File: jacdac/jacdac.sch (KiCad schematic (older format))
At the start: 6 parts, among them J1 Conn_02x03_Odd_Even, J2 Conn_02x03_Odd_Even

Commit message: update schematic to audio TRRS
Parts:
- removed J? (x3): AudioJackSwitch, symbol Connector:AudioJack3_Ground_Switch
- removed J?: AudioJack4_Ground, symbol Connector:AudioJack4_Ground
- added J3, J4, J5, J6: Audio_Jack_TRRS, Connectors:AUDIO-JACK-TRRS-SMD, symbol Connector:Audio_Jack_TRRS
- J1, J2: footprint (none) -> Pines:62000621121
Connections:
- wire segments 36 -> 39
- no-connect marks 7 -> 4

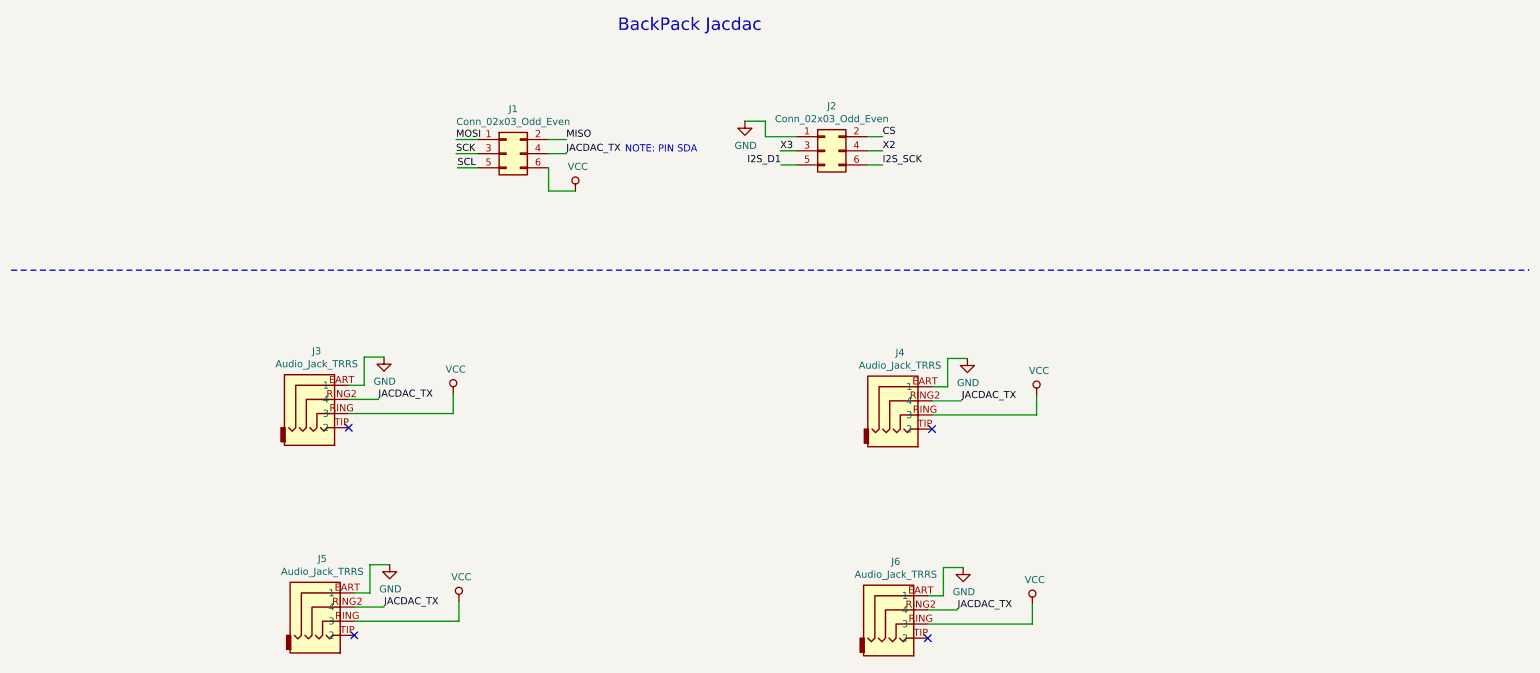
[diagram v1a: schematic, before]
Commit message: fix pin number jack TRRS
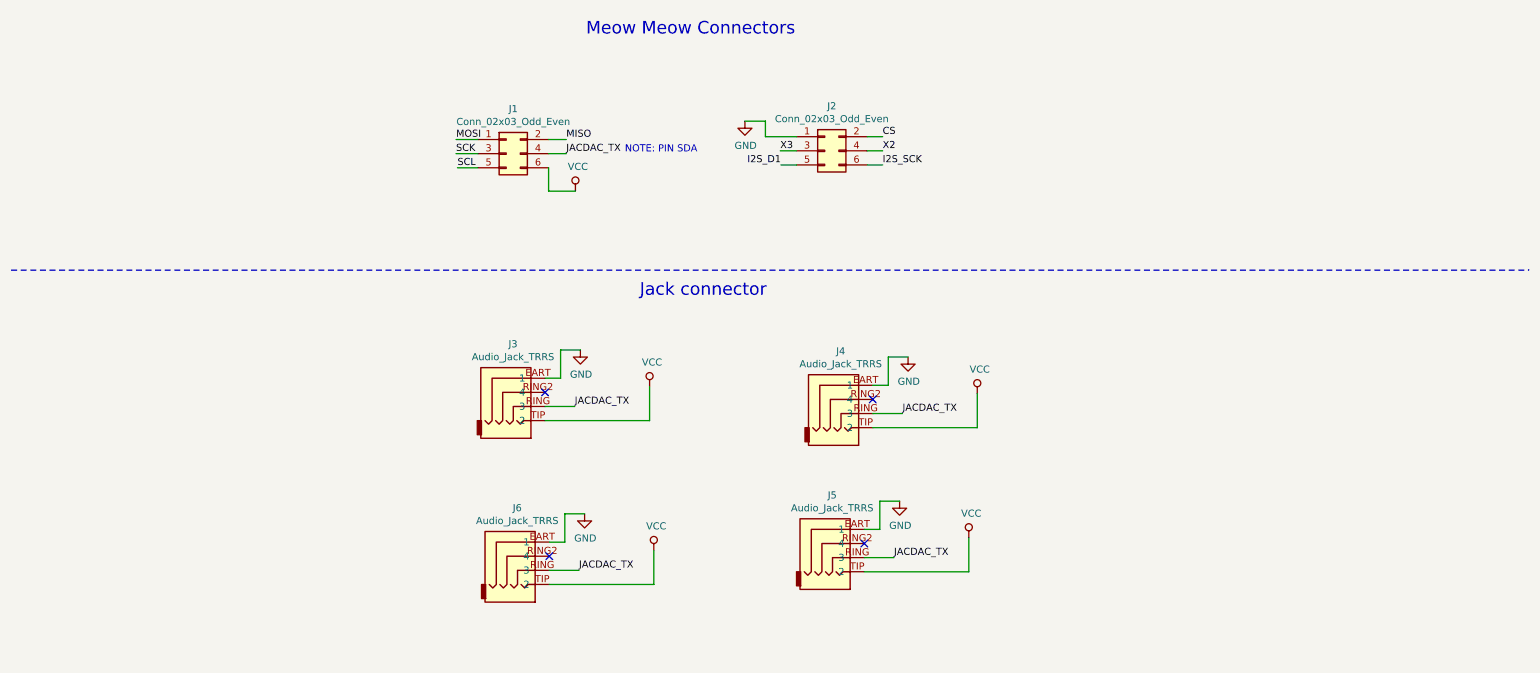
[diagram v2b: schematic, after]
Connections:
- net JACDAC_TX: now also J3.RING (3), J4.RING (3), J5.RING (3), J6.RING (3); no longer J3.RING2 (4), J4.RING2 (4), J5.RING2 (4), J6.RING2 (4)
- net VCC: now also J3.TIP (2), J4.TIP (2), J5.TIP (2), J6.TIP (2); no longer J3.RING (3), J4.RING (3), J5.RING (3), J6.RING (3)
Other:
- note added: "Jack connector"
- note added: "Meow Meow Connectors"
- note removed: "BackPack Jacdac"
- moved on the sheet: J3

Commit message: update pcb
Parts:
- J1: value Conn_02x03_Odd_Even -> Conn1
- J2: value Conn_02x03_Odd_Even -> Conn2
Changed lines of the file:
@@
 P 3965 1540
 F 0 "J1" H 4015 1857 50  0000 C CNN
-F 1 "Conn_02x03_Odd_Even" H 4015 1766 50  0000 C CNN
+F 1 "Conn1" H 4015 1766 50  0000 C CNN
 F 2 "Pines:62000621121" H 3965 1540 50  0001 C CNN
 F 3 "~" H 3965 1540 50  0001 C CNN
@@
 P 6220 1520
 F 0 "J2" H 6270 1837 50  0000 C CNN
-F 1 "Conn_02x03_Odd_Even" H 6270 1746 50  0000 C CNN
+F 1 "Conn2" H 6270 1746 50  0000 C CNN
 F 2 "Pines:62000621121" H 6220 1520 50  0001 C CNN
 F 3 "~" H 6220 1520 50  0001 C CNN

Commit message: new headers
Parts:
- J1, J2: footprint Pines:62000621121 -> Pines:61300621121
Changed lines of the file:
@@
 F 0 "J1" H 4015 1857 50  0000 C CNN
 F 1 "Conn1" H 4015 1766 50  0000 C CNN
-F 2 "Pines:62000621121" H 3965 1540 50  0001 C CNN
+F 2 "Pines:61300621121" H 3965 1540 50  0001 C CNN
 F 3 "~" H 3965 1540 50  0001 C CNN
 	1    3965 1540
@@
 F 0 "J2" H 6270 1837 50  0000 C CNN
 F 1 "Conn2" H 6270 1746 50  0000 C CNN
-F 2 "Pines:62000621121" H 6220 1520 50  0001 C CNN
+F 2 "Pines:61300621121" H 6220 1520 50  0001 C CNN
 F 3 "~" H 6220 1520 50  0001 C CNN
 	1    6220 1520

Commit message: init v0.2 add diodes and resistor
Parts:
- added D1, D2: MBR120, Diodes_SMD:D_SOD-123F, symbol Device:D_Schottky
- added R1: 100, Resistors_SMD:R_0805_HandSoldering, symbol Device:R_Small
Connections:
- net GND: now also D2.2 (A)
- net JACDAC_TX: now also R1.1; no longer J1.4 (Pin_4)
- net VCC: now also D1.1 (K)
- new net: D1.2 (A), D2.1 (K), J1.4 (Pin_4), R1.2
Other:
- note added: "NOTE: JACDAC_TX\nIS PIN SDA"
- note removed: "NOTE: PIN SDA"
- moved on the sheet: J2
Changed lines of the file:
@@
 Sheet 1 1
 Title "MeowMeow - Backpack JACDAC"
-Date "2018-12-25"
-Rev "0.1"
+Date "2019-02-25"
+Rev "0.2"
 Comp "Electronic Cats"
 Comment1 "Andres Sabas"
@@
 L Connector_Generic:Conn_02x03_Odd_Even J2
 U 1 1 5C2284F7
-P 6220 1520
-F 0 "J2" H 6270 1837 50  0000 C CNN
-F 1 "Conn2" H 6270 1746 50  0000 C CNN
-F 2 "Pines:61300621121" H 6220 1520 50  0001 C CNN
-F 3 "~" H 6220 1520 50  0001 C CNN
-	1    6220 1520
+P 7039 1520
+F 0 "J2" H 7089 1837 50  0000 C CNN
+F 1 "Conn2" H 7089 1746 50  0000 C CNN
+F 2 "Pines:61300621121" H 7039 1520 50  0001 C CNN
+F 3 "~" H 7039 1520 50  0001 C CNN
+	1    7039 1520
 	1    0    0    -1
 $EndComp
@@
 	4265 1440 4390 1440
 Wire Wire Line
-	4265 1540 4390 1540
-Wire Wire Line
-	6020 1520 5905 1520
-Wire Wire Line
-	6020 1620 5910 1620
-Wire Wire Line
-	6520 1420 6630 1420
-Wire Wire Line
-	6520 1520 6630 1520
-Wire Wire Line
-	6520 1620 6630 1620
+	6839 1520 6724 1520
+Wire Wire Line
+	6839 1620 6729 1620
+Wire Wire Line
+	7339 1420 7449 1420
+Wire Wire Line
+	7339 1520 7449 1520
+Wire Wire Line
+	7339 1620 7449 1620
 Text Label 3610 1440 0    50   ~ 0
 MOSI
@@
 Text Label 3610 1540 0    50   ~ 0
 SCK
-Text Label 4390 1540 0    50   ~ 0
+Text Label 5340 1541 0    50   ~ 0
 JACDAC_TX
 Text Label 3620 1640 0    50   ~ 0
 SCL
-Text Label 6630 1420 0    50   ~ 0
+Text Label 7449 1420 0    50   ~ 0
 CS
-Text Label 5905 1520 0    50   ~ 0
+Text Label 6724 1520 0    50   ~ 0
 X3
-Text Label 6630 1520 0    50   ~ 0
+Text Label 7449 1520 0    50   ~ 0
 X2
-Text Label 5910 1620 2    50   ~ 0
+Text Label 6729 1620 2    50   ~ 0
 I2S_D1
-Text Label 6630 1620 0    50   ~ 0
+Text Label 7449 1620 0    50   ~ 0
 I2S_SCK
 $Comp
 L power:GND #PWR0101
 U 1 1 5C235C6C
-P 5655 1310
-F 0 "#PWR0101" H 5655 1060 50  0001 C CNN
-F 1 "GND" H 5660 1137 50  0000 C CNN
-F 2 "" H 5655 1310 50  0001 C CNN
-F 3 "" H 5655 1310 50  0001 C CNN
-	1    5655 1310
-	1    0    0    -1
-$EndComp
-Wire Wire Line
-	5800 1420 6020 1420
+P 6474 1310
+F 0 "#PWR0101" H 6474 1060 50  0001 C CNN
+F 1 "GND" H 6479 1137 50  0000 C CNN
+F 2 "" H 6474 1310 50  0001 C CNN
+F 3 "" H 6474 1310 50  0001 C CNN
+	1    6474 1310
+	1    0    0    -1
+$EndComp
+Wire Wire Line
+	6619 1420 6839 1420
 $Comp
 L power:VCC #PWR0102
@@
 Meow Meow Connectors
 Wire Wire Line
-	5800 1420 5800 1310
-Wire Wire Line
-	5800 1310 5655 1310
+	6619 1420 6619 1310
+Wire Wire Line
+	6619 1310 6474 1310
 Wire Wire Line
 	4265 1640 4265 1805
 Wire Wire Line
 	4265 1805 4455 1805
-Text Notes 4805 1540 0    50   ~ 0
-NOTE: PIN SDA
+Text Notes 3764 2090 0    50   ~ 0
+NOTE: JACDAC_TX\nIS PIN SDA
 Wire Notes Line
 	460  2365 11205 2365
@@
 Text Notes 4910 2560 0    89   ~ 0
 Jack connector
+$Comp
+L Device:D_Schottky D2
+U 1 1 5C74169E
+P 4777 1775
+F 0 "D2" V 4731 1854 50  0000 L CNN
+F 1 "MBR120" V 4822 1854 50  0000 L CNN
+F 2 "Diodes_SMD:D_SOD-123F" H 4777 1775 50  0001 C CNN
+F 3 "~" H 4777 1775 50  0001 C CNN
+	1    4777 1775
+	0    1    1    0
+$EndComp
+$Comp
+L Device:D_Schottky D1
+U 1 1 5C741788
+P 4861 1284
+F 0 "D1" V 4815 1363 50  0000 L CNN
+F 1 "MBR120" V 4730 1357 50  0000 L CNN
+F 2 "Diodes_SMD:D_SOD-123F" H 4861 1284 50  0001 C CNN
+F 3 "~" H 4861 1284 50  0001 C CNN
+	1    4861 1284
+	0    1    1    0
+$EndComp
+$Comp
+L Device:R_Small R1
+U 1 1 5C741839
+P 5172 1541
+F 0 "R1" V 5110 1552 50  0000 C CNN
+F 1 "100" V 5247 1543 50  0000 C CNN
+F 2 "Resistors_SMD:R_0805_HandSoldering" H 5172 1541 50  0001 C CNN
+F 3 "~" H 5172 1541 50  0001 C CNN
+	1    5172 1541
+	0    1    1    0
+$EndComp
+Wire Wire Line
+	4777 1625 4777 1541
+Wire Wire Line
+	4265 1540 4777 1540
+Wire Wire Line
+	4777 1541 4861 1541
+Connection ~ 4777 1541
+Wire Wire Line
+	4777 1541 4777 1540
+Wire Wire Line
+	4861 1434 4861 1541
+Connection ~ 4861 1541
+Wire Wire Line
+	4861 1541 5072 1541
+Wire Wire Line
+	5272 1541 5340 1541
+Wire Wire Line
+	4777 1925 4777 1997
+Wire Wire Line
+	4861 1134 4861 1076
+$Comp
+L power:GND #PWR08
+U 1 1 5C74ED05
+P 4777 1997
+F 0 "#PWR08" H 4777 1747 50  0001 C CNN
+F 1 "GND" H 4782 1824 50  0000 C CNN
+F 2 "" H 4777 1997 50  0001 C CNN
+F 3 "" H 4777 1997 50  0001 C CNN
+	1    4777 1997
+	1    0    0    -1
+$EndComp
+$Comp
+L power:VCC #PWR07
+U 1 1 5C74EF54
+P 4861 1076
+F 0 "#PWR07" H 4861 926 50  0001 C CNN
+F 1 "VCC" H 4878 1249 50  0000 C CNN
+F 2 "" H 4861 1076 50  0001 C CNN
+F 3 "" H 4861 1076 50  0001 C CNN
+	1    4861 1076
+	1    0    0    -1
+$EndComp
 $EndSCHEMATC
